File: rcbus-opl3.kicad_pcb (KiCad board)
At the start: 2 copper layers, 100 x 50 mm, 35 parts, among them CON1 3.5mm jack, P1 RC2014 BUS, U1 74HCT688, U2 YMF262, U3 YAC512, U4 TL074, Y1 14.3181MHz

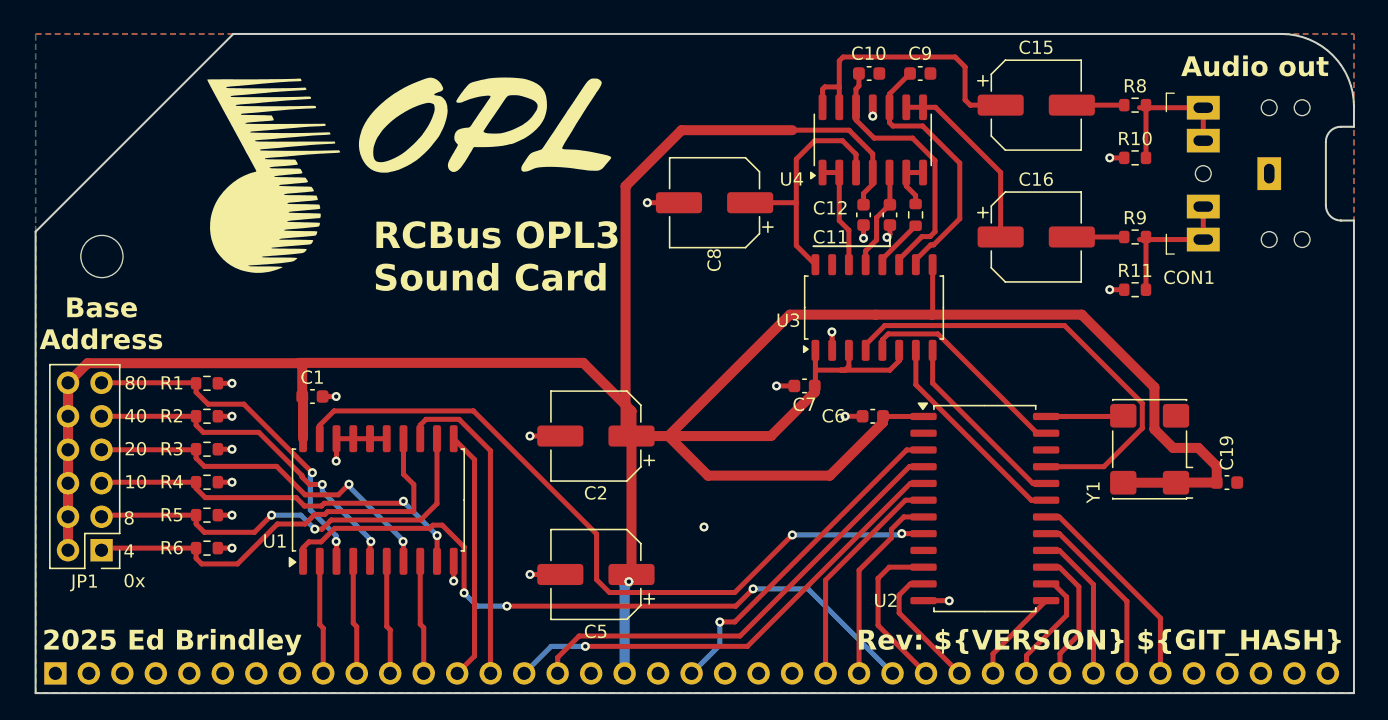
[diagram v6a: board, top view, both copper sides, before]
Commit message: increase spacing between tracks, remove opl4 pdf
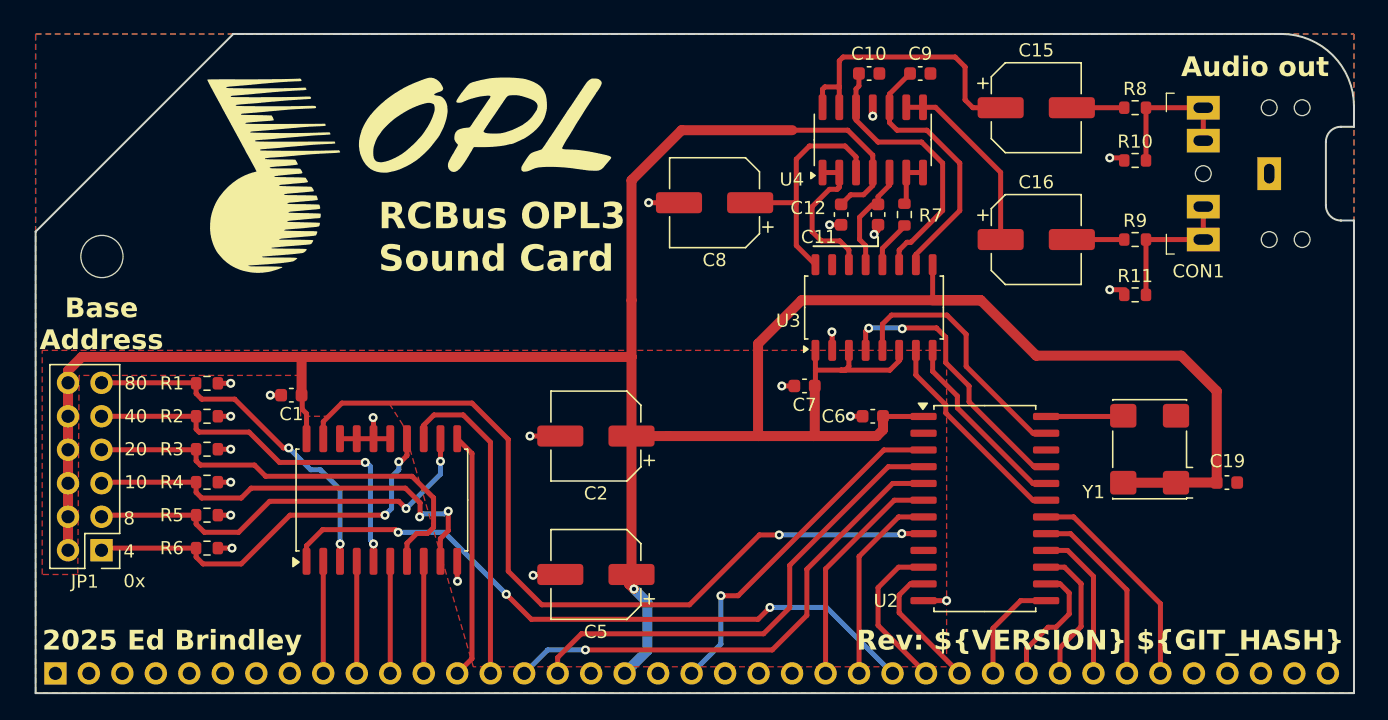
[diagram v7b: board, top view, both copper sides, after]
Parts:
- moved C12 1.70 mm to (121.1, 128.7)
- moved C1 1.60 mm to (79.4, 142.4), turned to 180 degrees
- moved C11 0.90 mm to (123.9, 128.7)
- moved R7 0.85 mm to (125.9, 128.7)
- moved R11 0.39 mm to (143.4, 134.8)
- moved U1 0.27 mm to (86.3, 150.3)
- moved C15 0.19 mm to (135.9, 120.6)
- moved C16 0.19 mm to (135.9, 130.6)
- moved R10 0.19 mm to (143.4, 124.6)
- moved R8 0.19 mm to (143.4, 120.6)
- moved R9 0.19 mm to (143.4, 130.6)
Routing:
- net /DOAB: track 34.4 -> 21.5 mm, vias 0 -> 2
- net +5V: track 242.3 -> 233.1 mm
- net /~{CS}: track 56.8 -> 61.8 mm
- net Net-(JP1-Pin_7): track 28.5 -> 33.3 mm, vias 2 -> 0
- net /DAC_CLK: track 15.8 -> 19.8 mm
- net Net-(JP1-Pin_5): track 29.6 -> 33.3 mm
- net Net-(JP1-Pin_9): track 26.7 -> 29.8 mm
- net Net-(U3-MP): track 8.56 -> 11.4 mm
- net /~{IORQ}: track 54.2 -> 51.4 mm
- net GND: track 32.0 -> 29.5 mm, vias 22 -> 21
- net /A1: track 36.3 -> 38.3 mm
- net /A0: track 34.9 -> 36.8 mm
- net Net-(JP1-Pin_1): track 32.0 -> 30.3 mm, vias 0 -> 2
- net Net-(JP1-Pin_3): track 33.0 -> 31.5 mm
- net /D2: track 7.18 -> 8.32 mm
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- added copper zone on F.Cu, net +5V

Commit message: remove 5v pour
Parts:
- moved C12 8.28 mm to (117.2, 121.4), turned to 90 degrees
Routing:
- net +5V: track 233.1 -> 229.1 mm
- net GND: track 29.5 -> 32.6 mm, vias 21 -> 23
- net Net-(U3-MP): track 11.4 -> 8.57 mm
- removed copper zone on F.Cu, net +5V
